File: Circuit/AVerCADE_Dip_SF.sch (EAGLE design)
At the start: 37 parts, among them IC1 MEGA8-P, K1 USB-B

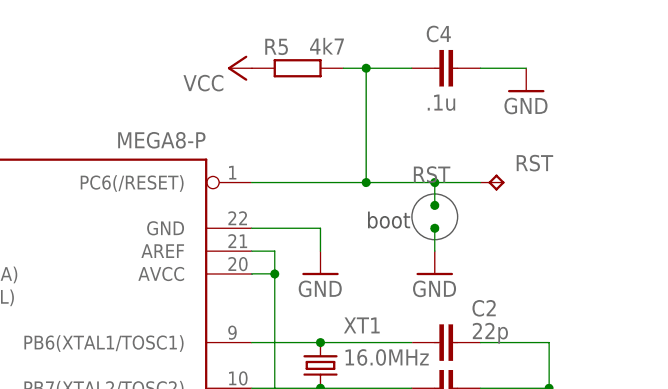
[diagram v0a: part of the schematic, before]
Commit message: Enhanced PTH board for homemade built.
The component pads have been enlarged to ease the home built versions of the board.
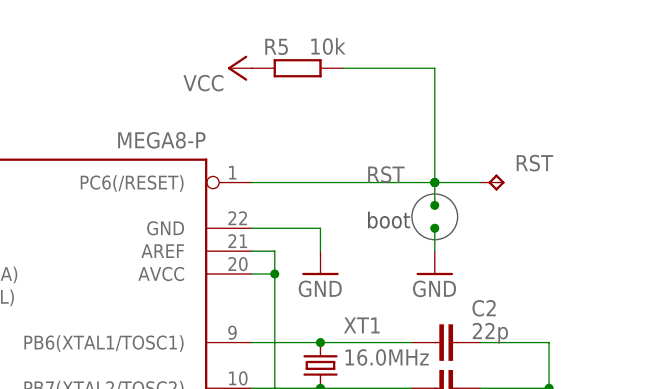
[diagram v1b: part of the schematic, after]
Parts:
- removed C4: .1u, rcl:C-EU050-024X044
- C1, C2: device rcl:C-EU025-024X044 -> rcl:C-EUC025-24X044L
- C3: device rcl:C-EU050-024X044 -> rcl:C-EUC050-025X075L
- D1, D2: device diode:ZENER-DIODEZD-5 -> diode:ZENER-DIODEZDIO-5L
- K1: device con-berg:PN61729-S -> con-berg:PN61729-SPN61729-SL
- LED1: device led:LED3MM -> led:LEDLED3MML
- R1, R2, R3, R4: device rcl:R-EU_0207/7 -> rcl:R-EU_0207/7L
- R5: value 4k7 -> 10k; device rcl:R-EU_0207/7 -> rcl:R-EU_0207/7L
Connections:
- net GND: no longer C4.2
- net RST: no longer C4.1
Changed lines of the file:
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@@
 <?xml version="1.0" encoding="utf-8"?>
 <!DOCTYPE eagle SYSTEM "eagle.dtd">
-<eagle version="7.4.0">
+<eagle version="7.3.0">
 <drawing>
 <settings>
@@
 <part name="B9" library="testpad" deviceset="TP" device="PAD1-13"/>
 <part name="XT1" library="crystal" deviceset="CRYSTAL" device="HC49U-V" value="16.0MHz"/>
-<part name="C1" library="rcl" deviceset="C-EU" device="025-024X044" value="22p"/>
-<part name="C2" library="rcl" deviceset="C-EU" device="025-024X044" value="22p"/>
-<part name="C3" library="rcl" deviceset="C-EU" device="050-024X044" value=".1u"/>
-<part name="R1" library="rcl" deviceset="R-EU_" device="0207/7" value="68"/>
-<part name="R2" library="rcl" deviceset="R-EU_" device="0207/7" value="68"/>
-<part name="R3" library="rcl" deviceset="R-EU_" device="0207/7" value="1k5"/>
-<part name="D1" library="diode" deviceset="ZENER-DIODE" device="ZD-5" value="3V3"/>
-<part name="D2" library="diode" deviceset="ZENER-DIODE" device="ZD-5" value="3V3"/>
+<part name="C1" library="rcl" deviceset="C-EU" device="C025-24X044L" value="22p"/>
+<part name="C2" library="rcl" deviceset="C-EU" device="C025-24X044L" value="22p"/>
+<part name="C3" library="rcl" deviceset="C-EU" device="C050-025X075L" value=".1u"/>
+<part name="R1" library="rcl" deviceset="R-EU_" device="0207/7L" value="68"/>
+<part name="R2" library="rcl" deviceset="R-EU_" device="0207/7L" value="68"/>
+<part name="R3" library="rcl" deviceset="R-EU_" device="0207/7L" value="1k5"/>
+<part name="D1" library="diode" deviceset="ZENER-DIODE" device="ZDIO-5L" value="3V3"/>
+<part name="D2" library="diode" deviceset="ZENER-DIODE" device="ZDIO-5L" value="3V3"/>
 <part name="GND4" library="supply1" deviceset="GND" device=""/>
 <part name="P+2" library="supply1" deviceset="VCC" device=""/>
-<part name="LED1" library="led" deviceset="LED" device="3MM"/>
-<part name="R4" library="rcl" deviceset="R-EU_" device="0207/7" value="2k2"/>
+<part name="LED1" library="led" deviceset="LED" device="LED3MML"/>
+<part name="R4" library="rcl" deviceset="R-EU_" device="0207/7L" value="2k2"/>
 <part name="GND5" library="supply1" deviceset="GND" device=""/>
 <part name="GND7" library="supply1" deviceset="GND" device=""/>
@@
 <part name="GND6" library="supply1" deviceset="GND" device=""/>
 <part name="FRAME2" library="frames" deviceset="A5L-LOC" device=""/>
-<part name="R5" library="rcl" deviceset="R-EU_" device="0207/7" value="4k7"/>
+<part name="R5" library="rcl" deviceset="R-EU_" device="0207/7L" value="10k"/>
 <part name="P+3" library="supply1" deviceset="VCC" device=""/>
-<part name="C4" library="rcl" deviceset="C-EU" device="050-024X044" value=".1u"/>
-<part name="GND10" library="supply1" deviceset="GND" device=""/>
-<part name="K1" library="con-berg" deviceset="PN61729-S" device="" value="USB-B"/>
+<part name="K1" library="con-berg" deviceset="PN61729-S" device="PN61729-SL" value="USB-B"/>
 <part name="IC1" library="atmel" deviceset="MEGA8-P" device=""/>
 <part name="VCC" library="testpad" deviceset="TP" device="PAD1-13"/>
@@
 <instance part="P+3" gate="VCC" x="137.16" y="119.38" smashed="yes" rot="R90">
 <attribute name="VALUE" x="132.08" y="116.84" size="1.778" layer="96"/>
-</instance>
-<instance part="C4" gate="G$1" x="160.02" y="119.38" smashed="yes" rot="R90">
-<attribute name="NAME" x="159.004" y="122.301" size="1.778" layer="95"/>
-<attribute name="VALUE" x="159.004" y="114.681" size="1.778" layer="96"/>
-</instance>
-<instance part="GND10" gate="1" x="170.18" y="116.84" smashed="yes">
-<attribute name="VALUE" x="167.64" y="114.3" size="1.778" layer="96"/>
 </instance>
 <instance part="K1" gate="G$1" x="25.4" y="78.74" rot="MR0"/>
@@
 </segment>
 <segment>
-<pinref part="C4" gate="G$1" pin="2"/>
-<pinref part="GND10" gate="1" pin="GND"/>
-<wire x1="170.18" y1="119.38" x2="165.1" y2="119.38" width="0.1524" layer="91"/>
-</segment>
-<segment>
 <pinref part="R4" gate="G$1" pin="1"/>
 <pinref part="GND9" gate="1" pin="GND"/>
@@
 <segment>
 <wire x1="160.02" y1="106.68" x2="160.02" y2="104.14" width="0.1524" layer="91"/>
-<wire x1="139.7" y1="106.68" x2="152.4" y2="106.68" width="0.1524" layer="91"/>
+<wire x1="139.7" y1="106.68" x2="160.02" y2="106.68" width="0.1524" layer="91"/>
 <junction x="160.02" y="104.14"/>
-<label x="157.48" y="106.68" size="1.778" layer="95"/>
+<label x="152.4" y="106.68" size="1.778" layer="95"/>
 <pinref part="R5" gate="G$1" pin="2"/>
-<wire x1="152.4" y1="106.68" x2="160.02" y2="106.68" width="0.1524" layer="91"/>
-<wire x1="149.86" y1="119.38" x2="152.4" y2="119.38" width="0.1524" layer="91"/>
-<wire x1="152.4" y1="119.38" x2="152.4" y2="106.68" width="0.1524" layer="91"/>
-<junction x="152.4" y="106.68"/>
-<pinref part="C4" gate="G$1" pin="1"/>
-<wire x1="157.48" y1="119.38" x2="152.4" y2="119.38" width="0.1524" layer="91"/>
-<junction x="152.4" y="119.38"/>
+<wire x1="149.86" y1="119.38" x2="160.02" y2="119.38" width="0.1524" layer="91"/>
+<wire x1="160.02" y1="119.38" x2="160.02" y2="106.68" width="0.1524" layer="91"/>
+<junction x="160.02" y="106.68"/>
 <pinref part="IC1" gate="G$1" pin="PC6(/RESET)"/>
 <pinref part="RST" gate="G$1" pin="TP"/>

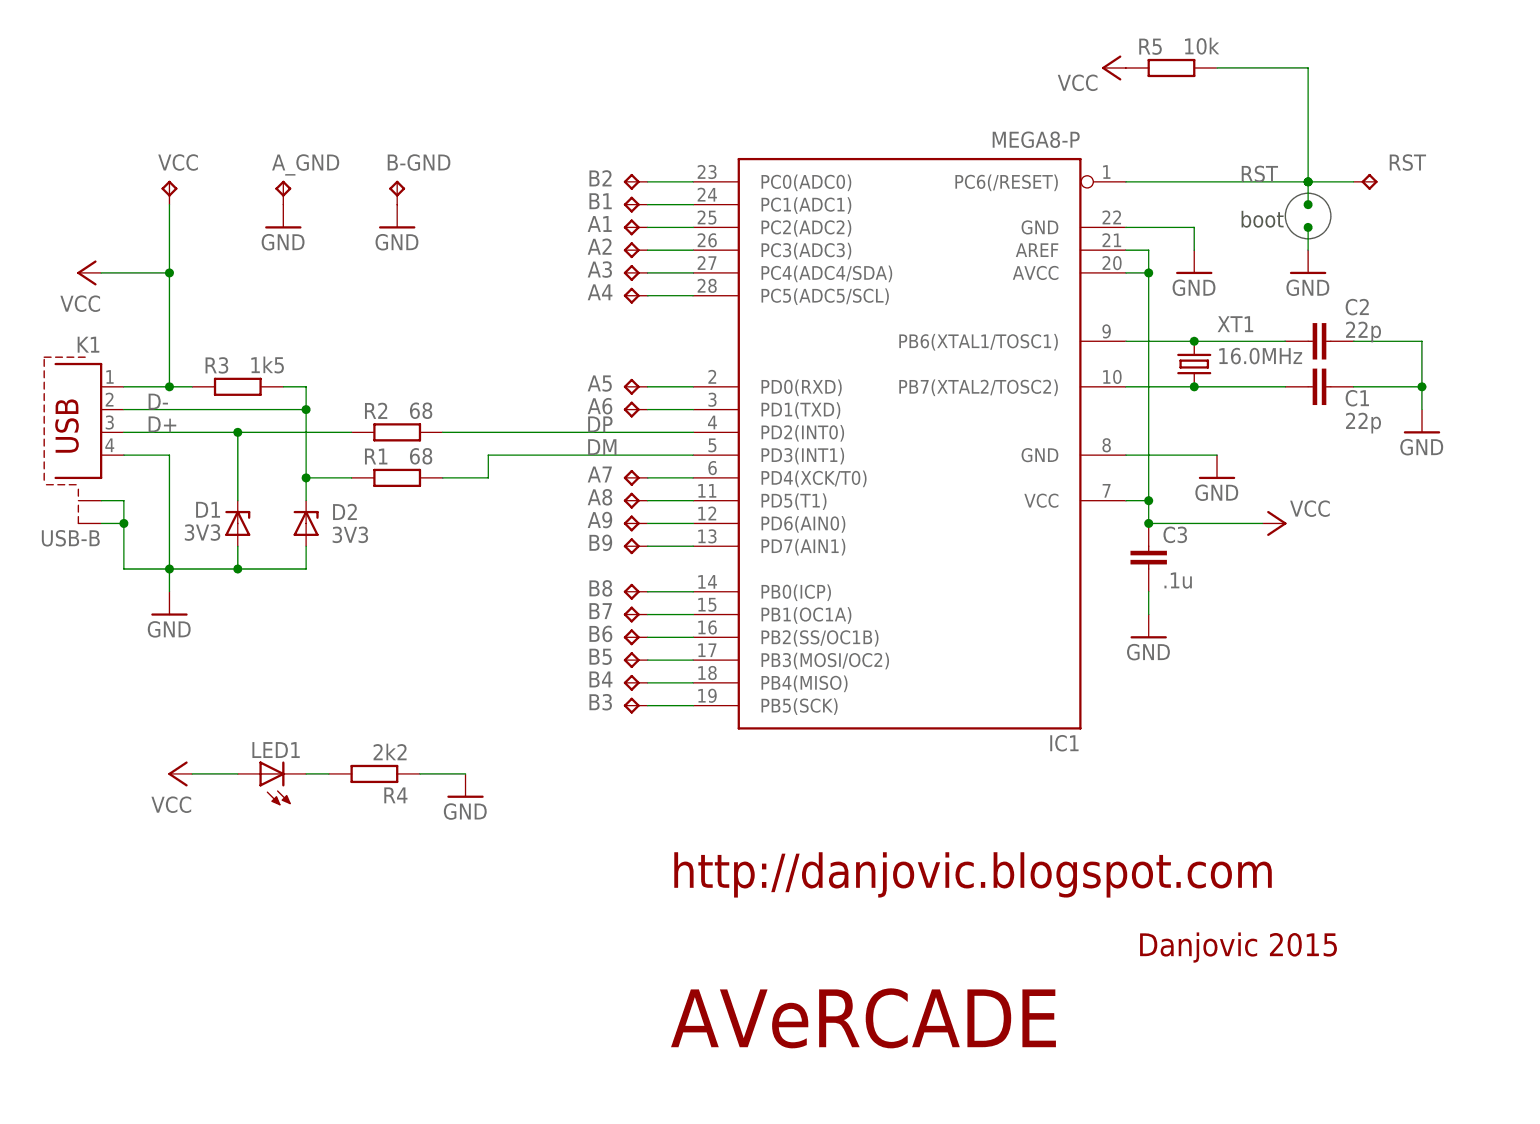
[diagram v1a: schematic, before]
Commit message: Added bootloader invoke button, increased clearance on LED pads
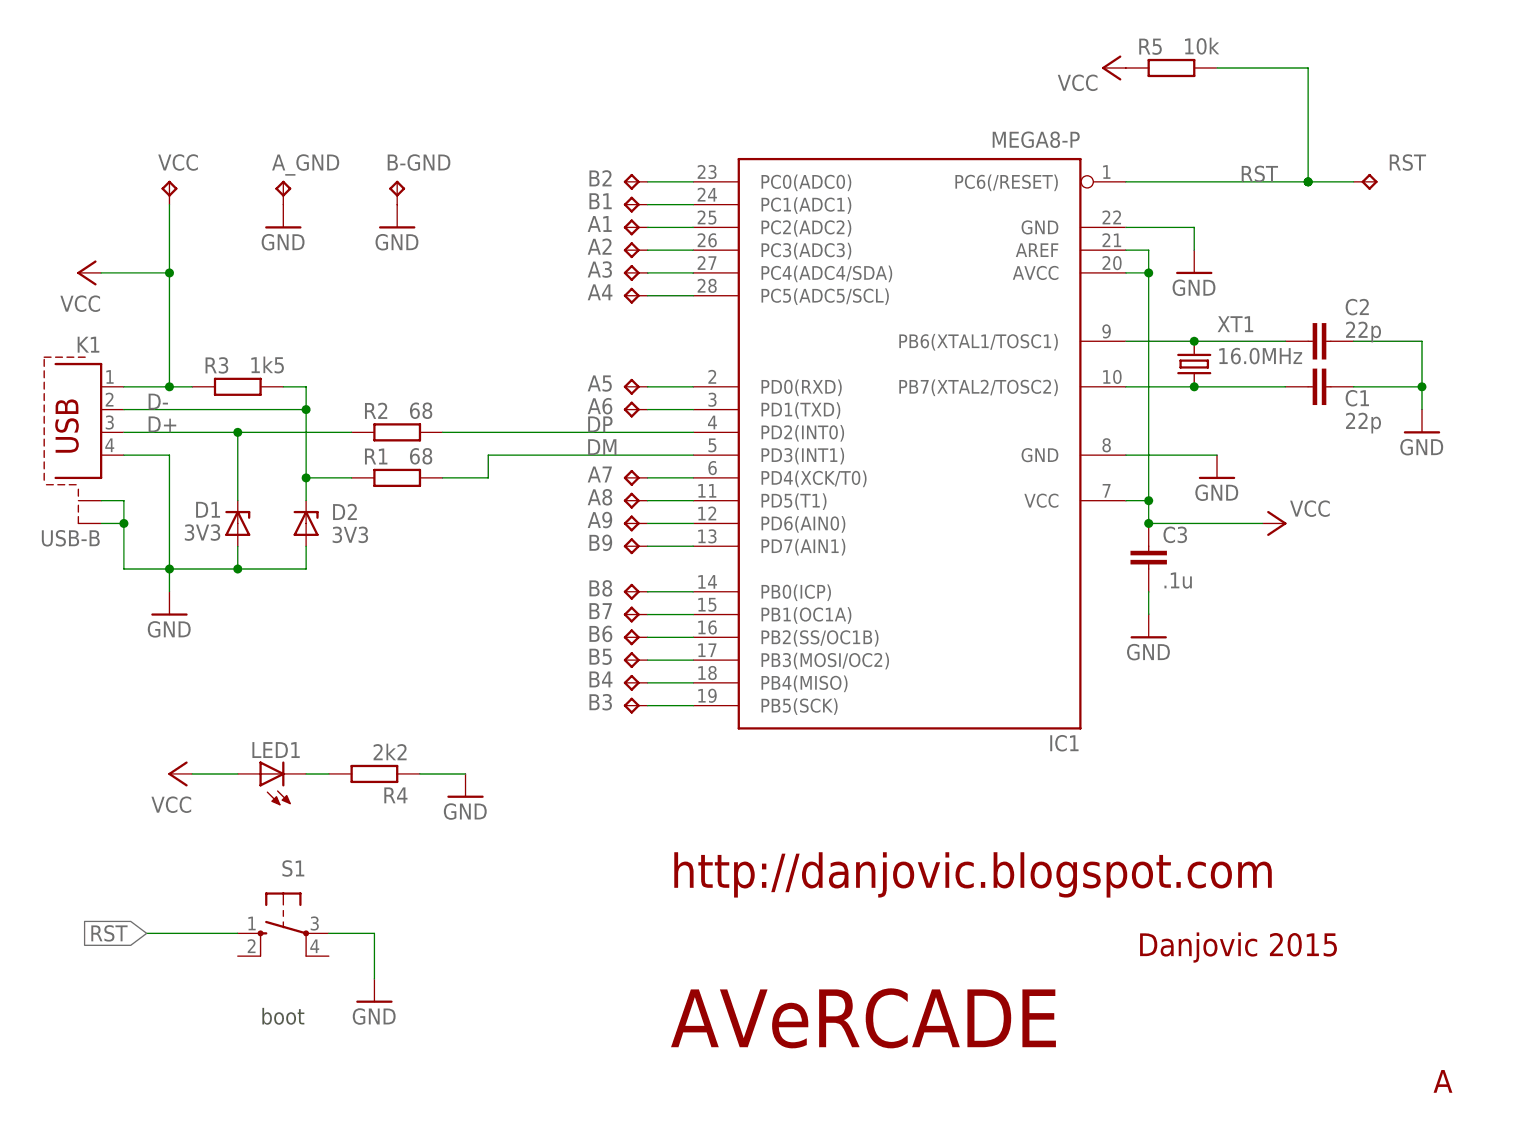
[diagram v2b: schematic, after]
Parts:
- added S1: (no value), switch-omron:10-XX
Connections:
- net GND: now also S1.P
- net RST: now also S1.S
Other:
- note added: "A"
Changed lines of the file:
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@@
 <?xml version="1.0" encoding="utf-8"?>
 <!DOCTYPE eagle SYSTEM "eagle.dtd">
-<eagle version="7.3.0">
+<eagle version="7.2.0">
 <drawing>
 <settings>
@@
 <part name="RST" library="testpad" deviceset="TP" device="PAD1-13"/>
 <part name="GND9" library="supply1" deviceset="GND" device=""/>
+<part name="S1" library="switch-omron" deviceset="10-XX" device=""/>
 </parts>
 <sheets>
 <sheet>
 <plain>
-<circle x="160.02" y="102.87" radius="2.54" width="0.1524" layer="97"/>
-<text x="152.4" y="101.6" size="1.778" layer="97">boot</text>
+<text x="43.18" y="12.7" size="1.778" layer="97">boot</text>
 <text x="140.97" y="20.32" size="2.54" layer="94" font="vector" ratio="14">Danjovic 2015</text>
 <text x="88.9" y="10.16" size="6.4516" layer="94" font="vector" ratio="14">AVeRCADE</text>
 <text x="88.9" y="27.94" size="3.81" layer="94" font="vector" ratio="14">http://danjovic.blogspot.com</text>
+<text x="173.99" y="5.08" size="2.54" layer="94" font="vector" ratio="14">A</text>
 </plain>
 <instances>
@@
 <attribute name="VALUE" x="35.56" y="38.1" size="1.778" layer="96" rot="R180"/>
 </instance>
-<instance part="GND6" gate="1" x="160.02" y="96.52" smashed="yes">
-<attribute name="VALUE" x="157.48" y="93.98" size="1.778" layer="96"/>
+<instance part="GND6" gate="1" x="55.88" y="15.24" smashed="yes">
+<attribute name="VALUE" x="53.34" y="12.7" size="1.778" layer="96"/>
 </instance>
 <instance part="FRAME2" gate="G$1" x="0" y="0" smashed="yes">
@@
 <attribute name="VALUE" x="63.5" y="35.56" size="1.778" layer="96"/>
 </instance>
+<instance part="S1" gate="1" x="45.72" y="22.86" rot="MR270"/>
 </instances>
 <busses>
@@
 </segment>
 <segment>
-<pinref part="GND6" gate="1" pin="GND"/>
-<wire x1="160.02" y1="99.06" x2="160.02" y2="101.6" width="0.1524" layer="91"/>
-<junction x="160.02" y="101.6"/>
-</segment>
-<segment>
 <pinref part="R4" gate="G$1" pin="1"/>
 <pinref part="GND9" gate="1" pin="GND"/>
 <wire x1="66.04" y1="40.64" x2="60.96" y2="40.64" width="0.1524" layer="91"/>
+</segment>
+<segment>
+<pinref part="S1" gate="1" pin="P"/>
+<pinref part="GND6" gate="1" pin="GND"/>
+<wire x1="50.8" y1="22.86" x2="55.88" y2="22.86" width="0.1524" layer="91"/>
+<wire x1="55.88" y1="22.86" x2="55.88" y2="17.78" width="0.1524" layer="91"/>
 </segment>
 </net>
@@
 <net name="RST" class="0">
 <segment>
-<wire x1="160.02" y1="106.68" x2="160.02" y2="104.14" width="0.1524" layer="91"/>
 <wire x1="139.7" y1="106.68" x2="160.02" y2="106.68" width="0.1524" layer="91"/>
-<junction x="160.02" y="104.14"/>
 <label x="152.4" y="106.68" size="1.778" layer="95"/>
 <pinref part="R5" gate="G$1" pin="2"/>
@@
 <junction x="160.02" y="106.68"/>
 </segment>
-</net>
+<segment>
+<wire x1="40.64" y1="22.86" x2="30.48" y2="22.86" width="0.1524" layer="91"/>
+<pinref part="S1" gate="1" pin="S"/>
+<label x="30.48" y="22.86" size="1.778" layer="95" rot="R180" xref="yes"/>
+</segment>
+</net>
